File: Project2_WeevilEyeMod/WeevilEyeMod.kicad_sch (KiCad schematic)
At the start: 8 parts, among them Q1 2N3904

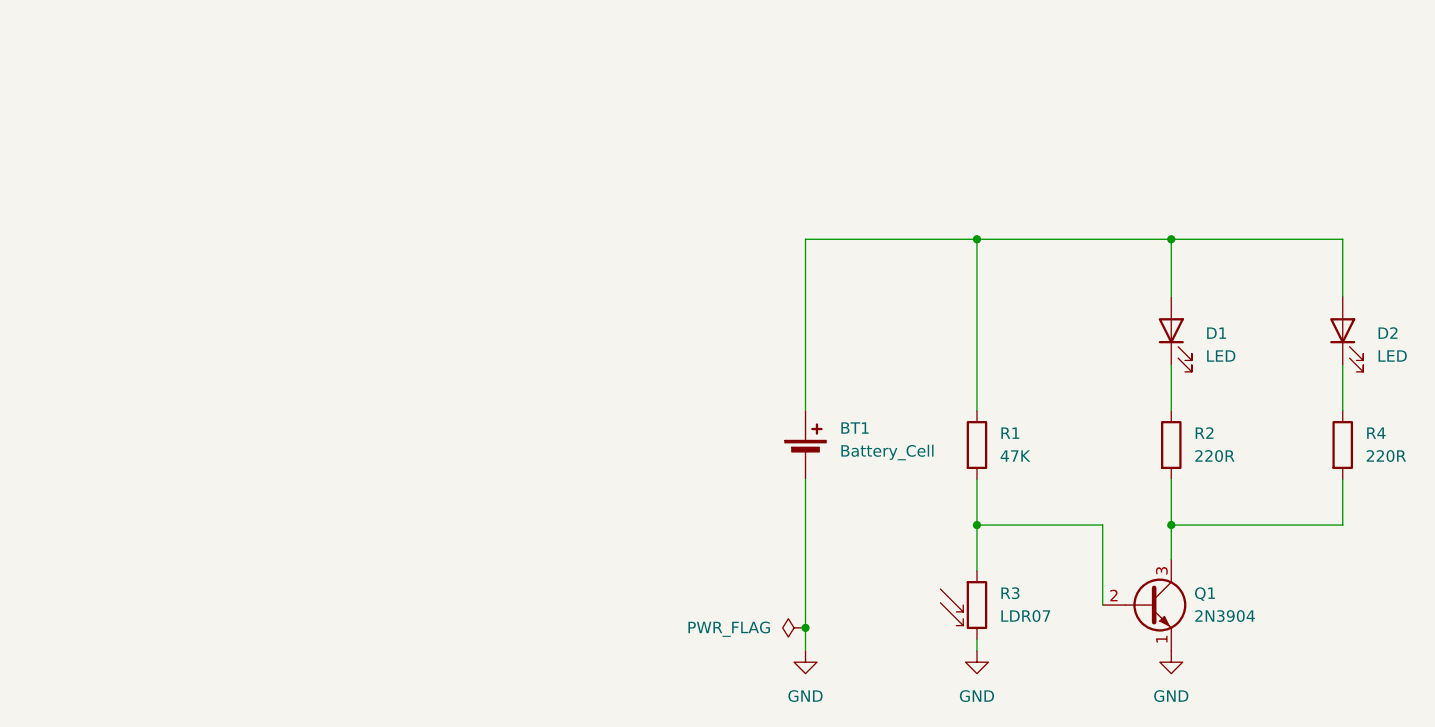
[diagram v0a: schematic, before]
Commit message: Updating plan for Session 3
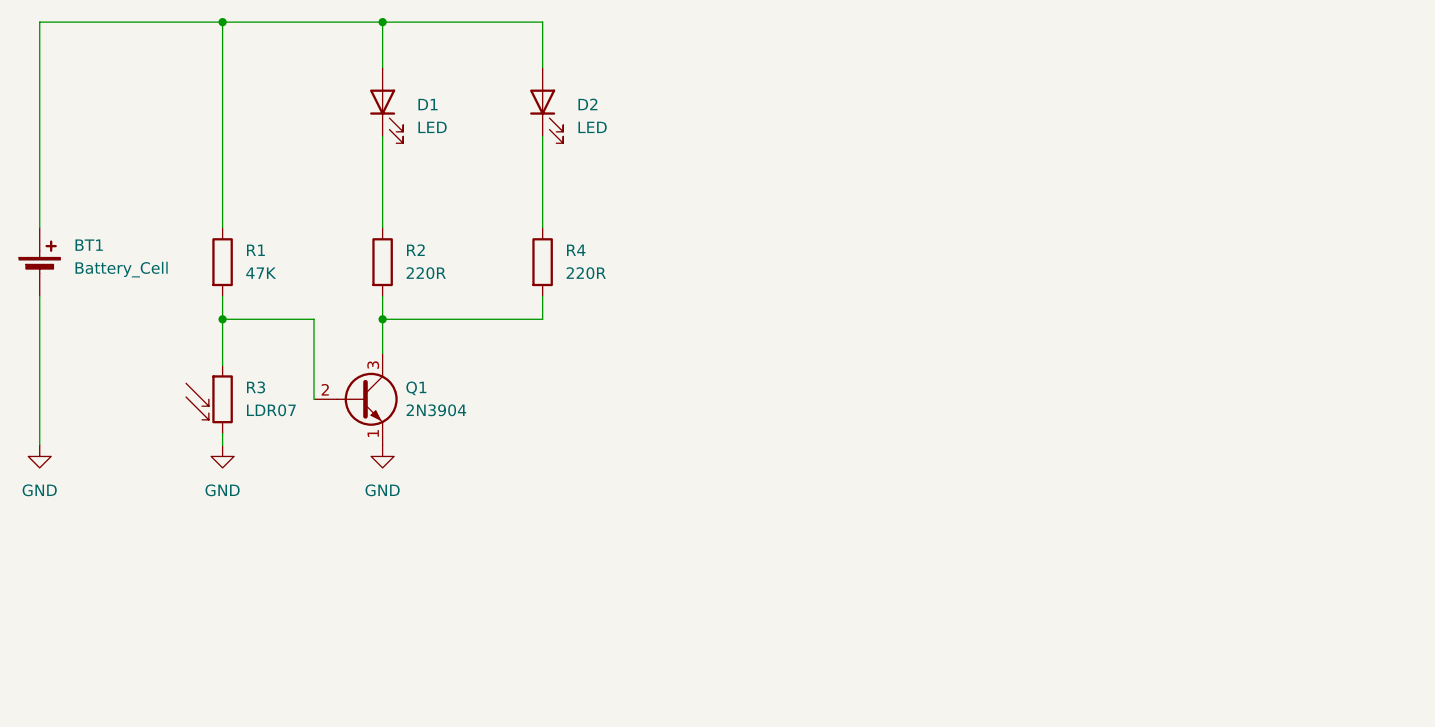
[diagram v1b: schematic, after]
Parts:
- BT1: footprint (none) -> Battery:BatteryHolder_ComfortableElectronic_CH273-2450_1x2450
- D1, D2: footprint (none) -> LED_THT:LED_D5.0mm
- Q1: footprint Package_TO_SOT_THT:TO-92_Inline -> Package_TO_SOT_THT:TO-92_Inline_Wide
- R1, R2, R4: footprint (none) -> Resistor_THT:R_Axial_DIN0204_L3.6mm_D1.6mm_P7.62mm_Horizontal
